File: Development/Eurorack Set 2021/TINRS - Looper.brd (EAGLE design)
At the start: 60.2 x 106.5 mm, 198 parts, among them IC1 74HC165D, IC2 TL074TSSOP14, IC3 NE5532D, IC4 MCP6004, IC5 74HC595BQ, IC6 74HC595BQ, IC7 74HC595BQ, IC8 74HC165D, J14 POWER_SIMPLE10, Q1 MMBT3904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

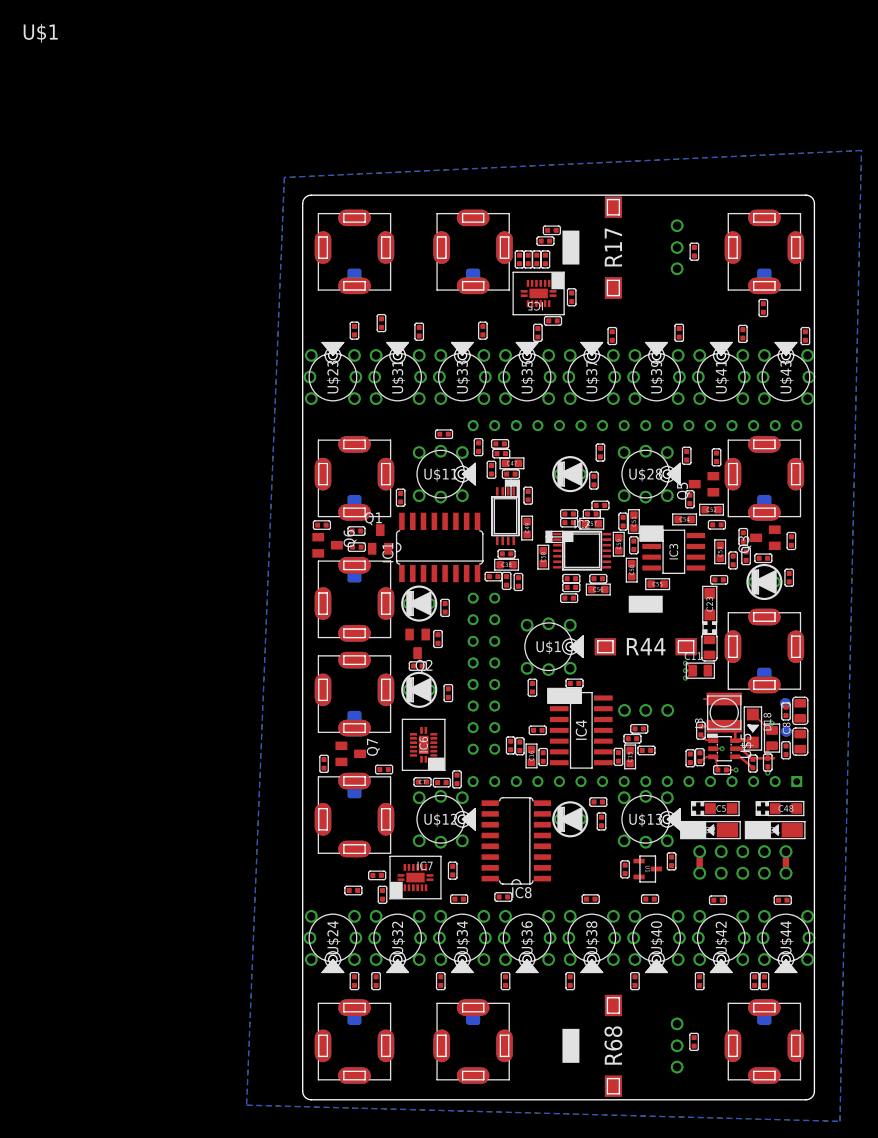
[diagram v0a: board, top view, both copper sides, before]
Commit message: looper orderable, wobbler adjustments, fenixcase power board
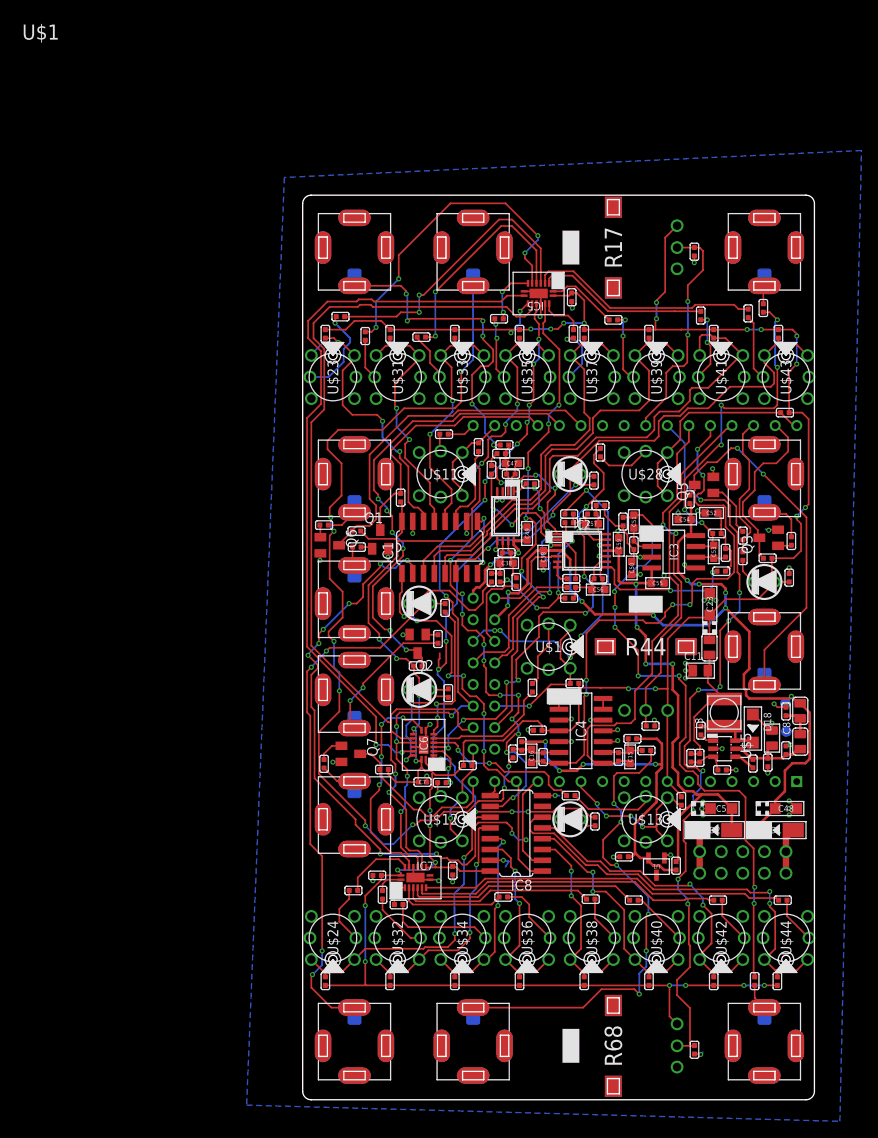
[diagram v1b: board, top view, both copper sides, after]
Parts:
- R15, R28: value 51k -> 100k
- moved C41 32.6 mm to (102.2, -56.3), turned to 0 degrees
- moved R58 27.7 mm to (113.7, -7.75), turned to 90 degrees
- moved R9 25.0 mm to (65.7, -8.13), turned to 0 degrees
- moved R54 21.4 mm to (108.1, -8.00), turned to 90 degrees
- moved R29 19.9 mm to (75.2, -10.5)
- moved R26 16.7 mm to (105.2, -72.8), turned to 270 degrees
- moved R92 12.6 mm to (118.0, -19.4), turned to 180 degrees
- moved R49 11.5 mm to (97.8, -8.51), turned to 180 degrees
- moved R38 10.7 mm to (84.3, -8.38)
- moved R45 9.36 mm to (93.1, -10.2), turned to 90 degrees
- moved R91 7.20 mm to (105.8, -65.2), turned to 270 degrees
- moved R35 7.14 mm to (72.5, -77.3)
- moved R51 3.56 mm to (102.0, -10.2)
- moved R13 3.45 mm to (63.9, -10.2)
- moved R25 3.44 mm to (71.5, -10.2)
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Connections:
- removed net N$1: U$55.P$9
- removed net N$19: U$55.P$10
- removed net N$26: U$55.P$12
- removed net N$41: U$55.P$19
- removed net N$47: U$55.P$2
- removed net N$53: U$55.P$3
- removed net N$54: U$55.P$4
- removed net N$55: U$55.P$5
- net 1_1_BUT: now also IC1.14; no longer IC1.11
- net 1_1_LED: now also IC5.4; no longer IC5.15
- net 1_2_BUT: now also IC1.13; no longer IC1.12
- net 1_2_LED: now also IC5.6; no longer IC5.1
- net 1_3_BUT: now also IC1.12; no longer IC1.13
- net 1_3_LED: now also IC5.5; no longer IC5.2
- net 1_4_BUT: now also IC1.11; no longer IC1.14
- net 1_4_LED: now also IC5.7; no longer IC5.3
- net 1_5_LED: now also IC5.15; no longer IC5.4
- net 1_6_LED: now also IC5.1; no longer IC5.5
- net 1_7_LED: now also IC5.2; no longer IC5.6
- net 1_8_LED: now also IC5.3; no longer IC5.7
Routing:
- net 3.3V: track 0.00 -> 365.2 mm, vias 0 -> 31
- net CLOCK: track 0.00 -> 116.1 mm, vias 0 -> 2
- net N$33: track 0.00 -> 108.9 mm, vias 0 -> 9
- net 12V: track 0.00 -> 99.2 mm, vias 0 -> 10
- net KNOB_BALANCE_2: track 0.00 -> 89.2 mm, vias 0 -> 9
- net SHIFTER1TO2: track 0.00 -> 86.3 mm, vias 0 -> 2
- net LATCH: track 0.00 -> 86.0 mm, vias 0 -> 13
- net INP_CLK: track 0.00 -> 83.1 mm, vias 0 -> 10
- net GND: track 11.3 -> 94.0 mm, vias 7 -> 63
- net N$88: track 0.00 -> 74.9 mm, vias 0 -> 8
- net N$108: track 0.00 -> 73.9 mm, vias 0 -> 4
- net ADC_BALANCE_1: track 0.00 -> 66.2 mm, vias 0 -> 6
- net 1_8_BUT: track 0.00 -> 61.3 mm, vias 0 -> 2
- net 1_7_BUT: track 0.00 -> 59.3 mm
- net -12V: track 0.00 -> 58.2 mm, vias 0 -> 4
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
